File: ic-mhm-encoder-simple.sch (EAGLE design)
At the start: 35 parts, among them IC1 LS7183-SOIC, J1 2023960907, J2 2023960607, M1 BSS670S2LH6327XTSA1, SW1 CS-4-13NTA, U1 24LC16BT-I/MC, U2 1SS308(TE85L,F, U3 1SS308(TE85L,F, U4 1SS308(TE85L,F

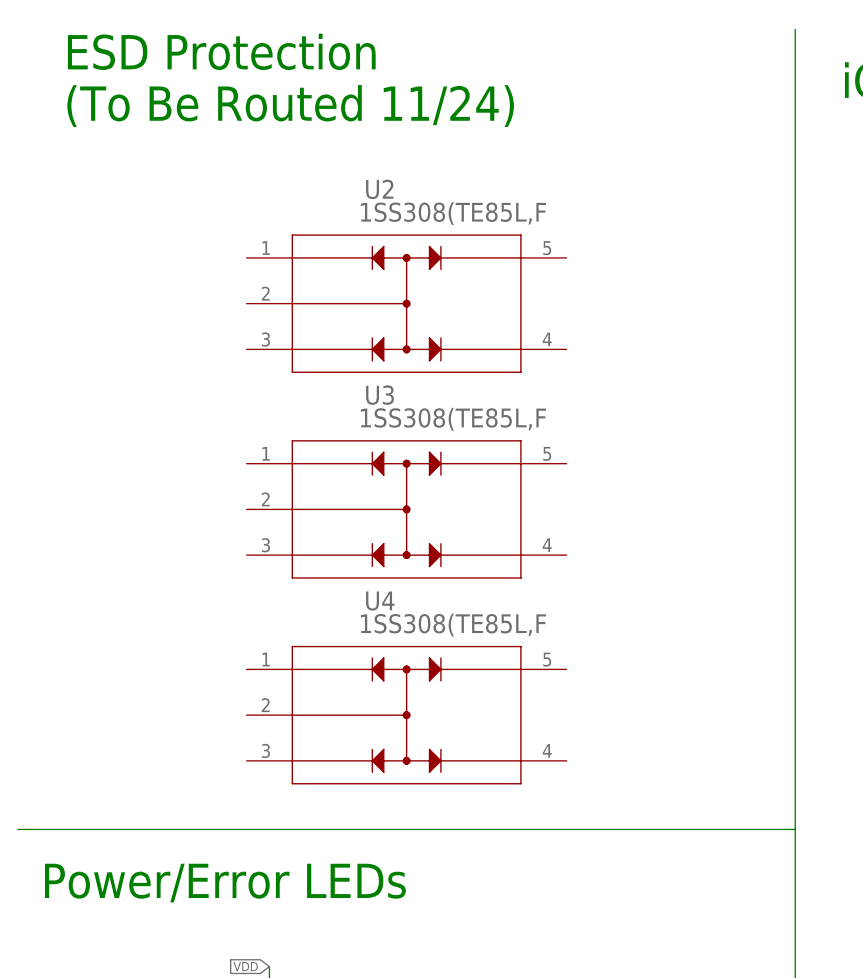
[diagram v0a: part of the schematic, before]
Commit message: Routed ESD Diodes
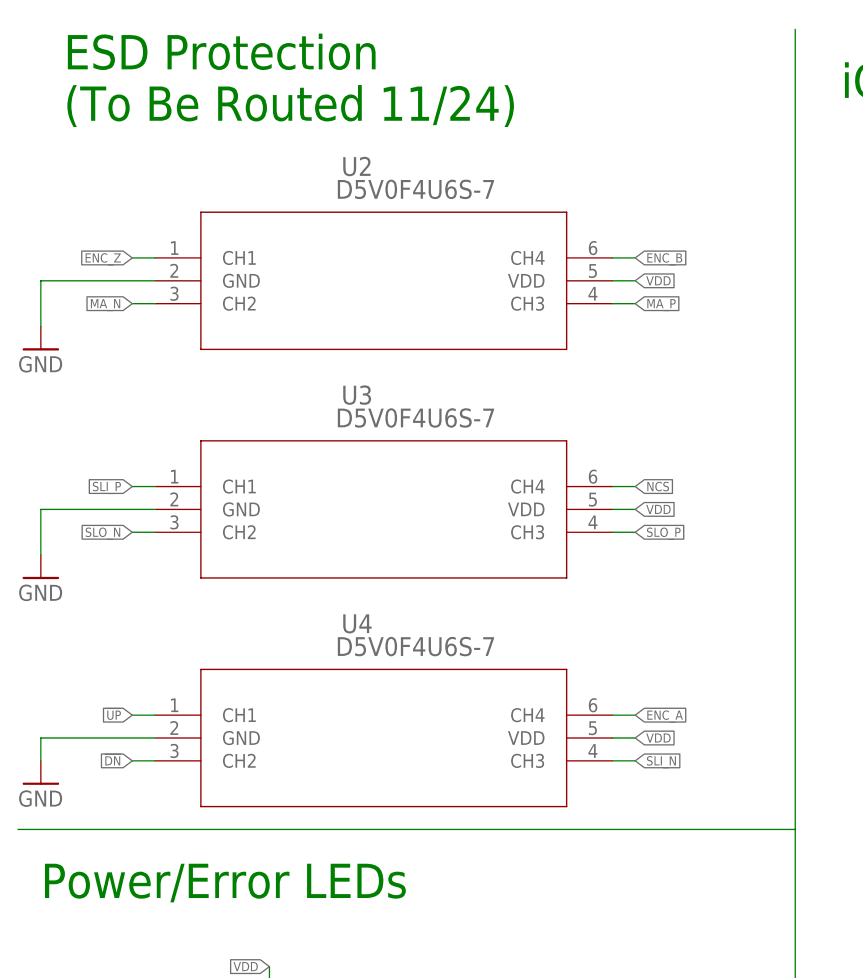
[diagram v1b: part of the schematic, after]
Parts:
- U2, U3, U4: value 1SS308(TE85L,F -> D5V0F4U6S-7; device ic-mhm:1SS308(TE85L,F -> ic-mhm:D5V0F4U6S-7
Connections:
- net !DN: now also U4.CH2
- net !UP: now also U4.CH1
- net ENC_A: now also U4.CH4
- net ENC_B: now also U2.CH4
- net ENC_Z: now also U2.CH1
- net GND: now also U2.GND, U3.GND, U4.GND
- net MA_N: now also U2.CH2
- net MA_P: now also U2.CH3
- net NCS: now also U3.CH4
- net SLI_N: now also U4.CH3
- net SLI_P: now also U3.CH1
- net SLO_N: now also U3.CH2
- net SLO_P: now also U3.CH3
- net VDD: now also U2.VDD, U3.VDD, U4.VDD

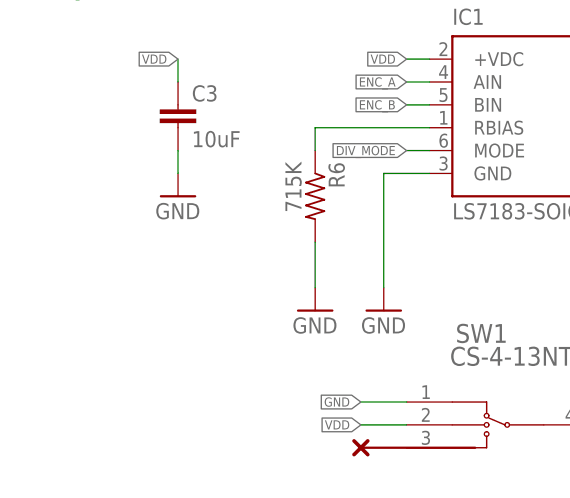
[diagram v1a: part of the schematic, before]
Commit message: changed RBIAS and added note about range
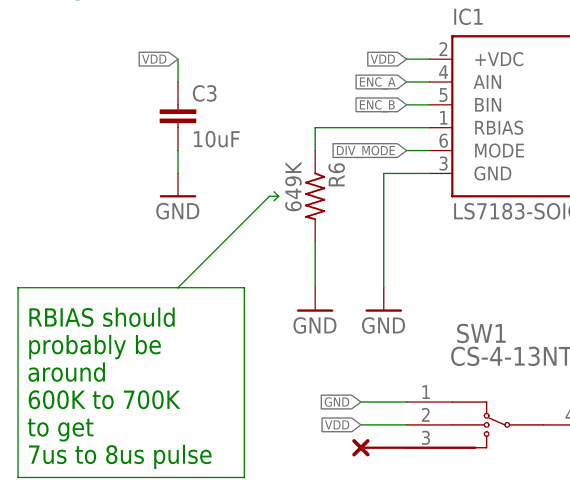
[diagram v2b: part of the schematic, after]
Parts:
- R6: value 715K -> 649K
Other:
- note added: "RBIAS should probably be around 600K to 700K to get 7us to 8us pulse"
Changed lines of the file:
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@@
 <part name="GND7" library="supply1" library_urn="urn:adsk.eagle:library:371" deviceset="GND" device=""/>
 <part name="GND8" library="supply1" library_urn="urn:adsk.eagle:library:371" deviceset="GND" device=""/>
-<part name="R6" library="rcl" library_urn="urn:adsk.eagle:library:334" deviceset="R-US_" device="R0603" package3d_urn="urn:adsk.eagle:package:23555/3" value="715K"/>
+<part name="R6" library="rcl" library_urn="urn:adsk.eagle:library:334" deviceset="R-US_" device="R0603" package3d_urn="urn:adsk.eagle:package:23555/3" value="649K"/>
 <part name="GND9" library="supply1" library_urn="urn:adsk.eagle:library:371" deviceset="GND" device=""/>
 <part name="SW1" library="ic-mhm" library_urn="urn:adsk.eagle:library:32396126" deviceset="CS-4-13NTA" device="" package3d_urn="urn:adsk.eagle:package:32411948/3"/>
@@
 <text x="228.6" y="43.18" size="3.81" layer="91" ratio="14" rot="R90">Absolute</text>
 <text x="228.6" y="81.28" size="3.81" layer="91" ratio="14" rot="R90">Incremental</text>
+<text x="6.096" y="3.302" size="2.032" layer="91">RBIAS should
+probably be
+around
+600K to 700K
+to get
+7us to 8us pulse</text>
 </plain>
 <instances>
@@
 </segment>
 </net>
+<net name="N$7" class="0">
+<segment>
+<wire x1="33.02" y1="33.02" x2="22.86" y2="22.86" width="0.1524" layer="91"/>
+<wire x1="22.86" y1="22.86" x2="5.08" y2="22.86" width="0.1524" layer="91"/>
+<wire x1="5.08" y1="22.86" x2="5.08" y2="1.778" width="0.1524" layer="91"/>
+<wire x1="5.08" y1="1.778" x2="30.226" y2="1.778" width="0.1524" layer="91"/>
+<wire x1="30.226" y1="1.778" x2="30.226" y2="22.86" width="0.1524" layer="91"/>
+<wire x1="30.226" y1="22.86" x2="22.86" y2="22.86" width="0.1524" layer="91"/>
+<wire x1="33.02" y1="33.02" x2="34.036" y2="33.02" width="0.1524" layer="91"/>
+<wire x1="33.528" y1="32.512" x2="34.036" y2="33.02" width="0.1524" layer="91"/>
+<wire x1="34.036" y1="33.02" x2="33.528" y2="33.528" width="0.1524" layer="91"/>
+</segment>
+</net>
